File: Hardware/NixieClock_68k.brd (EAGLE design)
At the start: 100 x 100 mm, 80 parts, among them IC1 68008, IC10 7805, IC11 MIC803, IC2 AS6C1008, IC3 39SF020, IC4 DS1244Y, IC5 FT245R, IC6 NE555, IC7 ATF1504AS, IC8 74HC377N, IC9 74HC373N, Q1 2N4401

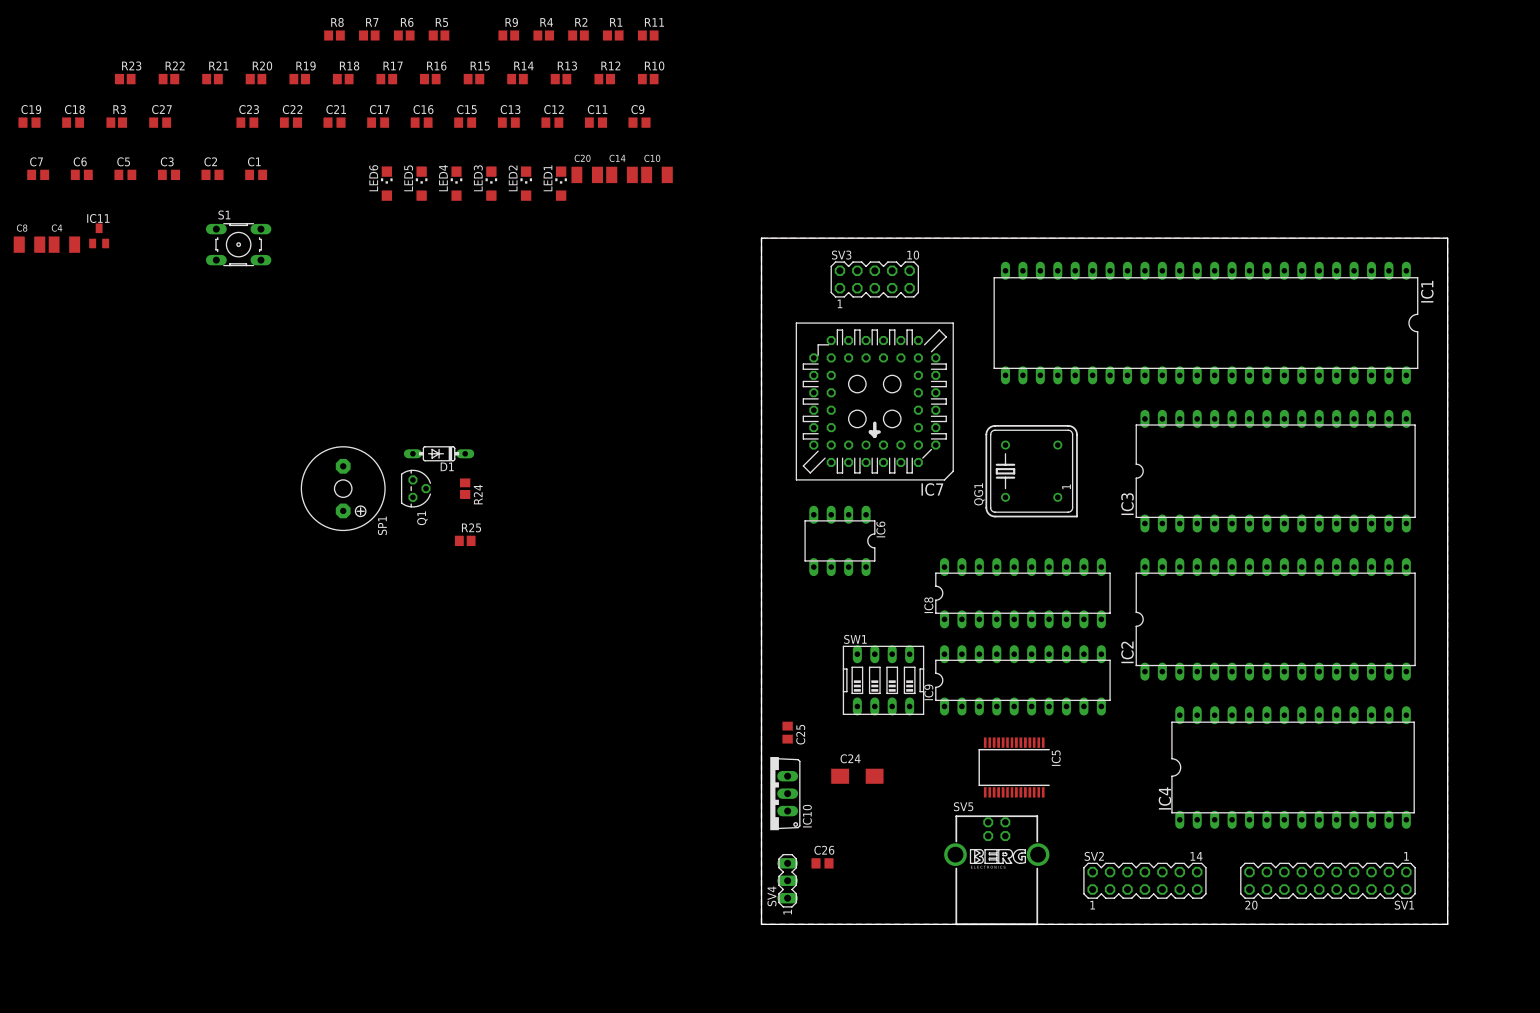
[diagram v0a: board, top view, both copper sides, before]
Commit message: more progress routing board
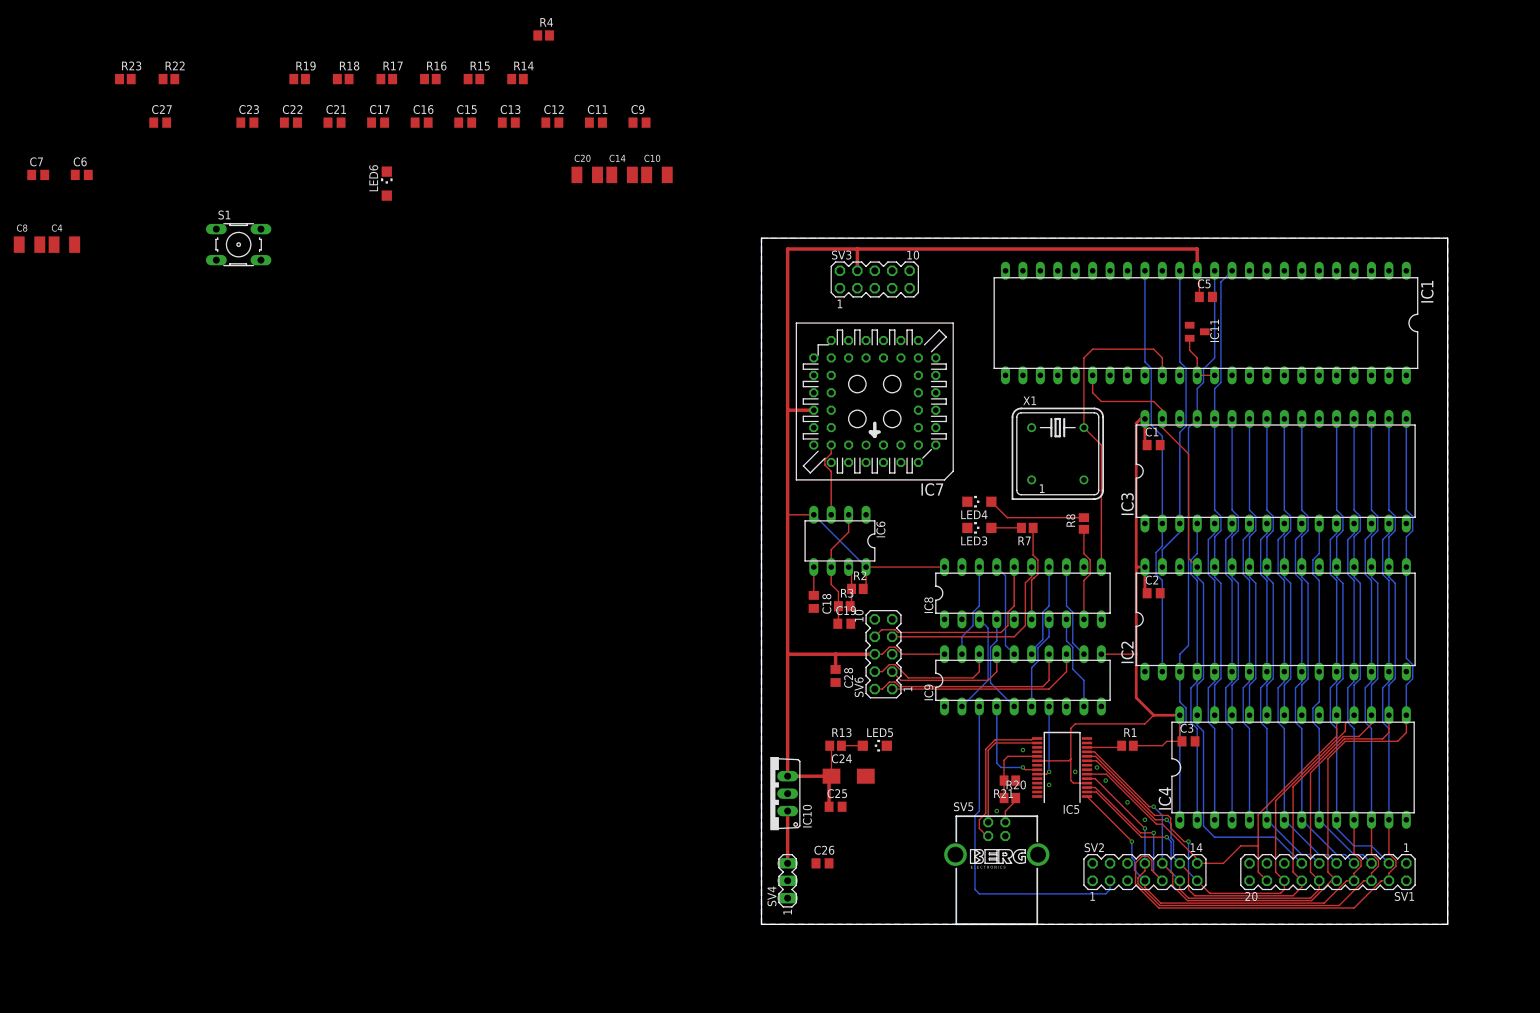
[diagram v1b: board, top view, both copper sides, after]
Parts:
- removed D1: 1N4148, diode:DO35-7
- removed LED1, LED2: (no value), led:CHIPLED_1206
- removed Q1: 2N4401, transistor-npn:TO92
- removed QG1: 4MHz, crystal:DIL08S
- removed R10, R11, R12, R9: 10k, rcl:R2012
- removed R24, R25: 1k, rcl:R2012
- removed R5, R6: 3k, rcl:R2012
- removed SP1: KSS1201, buzzer:KSS1201
- removed SW1: (no value), special:EDG-04
- added C28: 100nF, rcl:C0805
- added SV6: (no value), con-lstb:MA05-2
- added X1: 4MHz, crystal:DIL08S
- moved C3 170.0 mm to (62.2, 26.7)
- moved IC11 160.6 mm to (63.5, 86.4), turned to 270 degrees
- moved C5 158.5 mm to (64.8, 91.4)
- moved R21 154.8 mm to (36.2, 21.0), turned to 180 degrees
- moved R20 151.8 mm to (36.2, 18.4)
- moved C2 150.1 mm to (57.1, 48.3)
- moved C19 139.4 mm to (12.1, 43.8)
- moved C1 136.6 mm to (57.1, 69.8)
- moved R8 130.3 mm to (47.0, 58.4), turned to 90 degrees
- moved C18 128.6 mm to (7.62, 47.0), turned to 270 degrees
- moved R1 127.8 mm to (53.3, 26.0)
- moved R3 127.3 mm to (12.1, 46.4)
- moved R7 119.8 mm to (38.7, 57.8), turned to 180 degrees
- moved LED5 105.2 mm to (16.5, 26.0), turned to 270 degrees
- moved R13 105.1 mm to (10.8, 26.0)
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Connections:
- removed net !IO_OUT_EN: IC7.25
- removed net BEEPER: IC8.16, R24.1
- removed net CFG0: IC9.13, R9.1, SW1.5
- removed net CFG1: IC9.14, R10.1, SW1.6
- removed net CFG2: IC9.17, R11.1, SW1.7
- removed net CFG3: IC9.18, R12.1, SW1.8
- removed net JTAG_TCK: IC7.32
- removed net JTAG_TDI: IC7.7
- removed net JTAG_TDO: IC7.38
- removed net JTAG_TMS: IC7.13
- removed net N$11: Q1.2, R24.2
- removed net N$12: D1.A, Q1.1, SP1.-
- removed net N$13: D1.C, R25.1
- removed net N$3: LED1.A, R5.2
- removed net N$5: LED2.A, R6.2
- removed net VPA: R22.1
- new net OUT0: IC8.16, SV6.8
- new net OUT1: IC8.15, SV6.7
- new net SW0: IC9.13, SV6.1
- new net SW1: IC9.14, SV6.2
- new net SW2: IC9.17, SV6.3
- new net SW3: IC9.18, SV6.4
- net !IO_OUT_CS: now also IC7.25
- net !VPA: now also R22.1
- net +5V: now also C28.1, SV6.6, X1.8; no longer QG1.8, R10.2, R11.2, R12.2, R25.2, R9.2, SP1.+
- net CLK: now also X1.5; no longer QG1.5
- net CPLD_TCK: now also IC7.32
- net CPLD_TDI: now also IC7.7
- net CPLD_TDO: now also IC7.38
- net CPLD_TMS: now also IC7.13
- net D0: now also SV1.8; no longer SV1.4
- net D2: now also SV1.4; no longer SV1.8
- net GND: now also C28.2, IC9.8, SV6.5, X1.4; no longer LED1.C, LED2.C, Q1.3, QG1.4, SW1.1, SW1.2, SW1.3, SW1.4
- net STATUS0: no longer R5.1
- net STATUS1: no longer R6.1
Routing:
- net +5V: track 0.00 -> 323.9 mm
- net D3: track 0.00 -> 144.0 mm, vias 0 -> 1
- net D2: track 0.00 -> 137.9 mm, vias 0 -> 1
- net D4: track 0.00 -> 136.5 mm, vias 0 -> 1
- net D5: track 0.00 -> 134.2 mm, vias 0 -> 1
- net D6: track 0.00 -> 129.8 mm, vias 0 -> 1
- net D1: track 0.00 -> 125.7 mm, vias 0 -> 1
- net D7: track 0.00 -> 119.6 mm
- net D0: track 0.00 -> 118.7 mm, vias 0 -> 1
- net R/!W!: track 0.00 -> 94.2 mm
- net A14: track 0.00 -> 82.9 mm
- net A13: track 0.00 -> 67.3 mm
- net A16: track 0.00 -> 60.2 mm
- net A0: track 0.00 -> 55.7 mm
- net A4: track 0.00 -> 54.9 mm
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
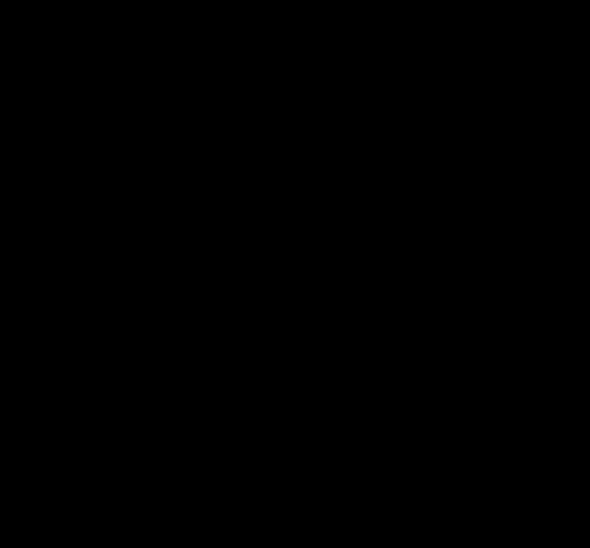
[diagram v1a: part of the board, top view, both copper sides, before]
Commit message: added some more missing pull resistors for usb
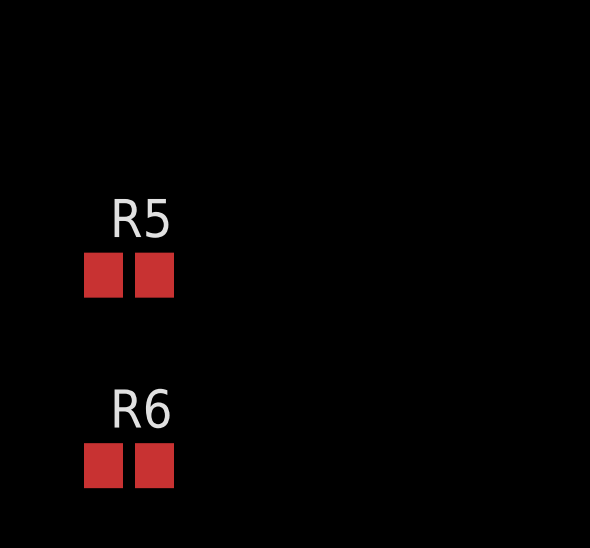
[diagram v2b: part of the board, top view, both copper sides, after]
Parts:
- added R5, R6: 10k, rcl:R2012
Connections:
- net !USB_RXF: now also R6.1
- net !USB_TXE: now also R5.1
- net +5V: now also R6.2
- net GND: now also R5.2
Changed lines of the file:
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@@
 <attribute name="VALUE" x="8.255" y="37.465" size="1.27" layer="27" rot="R270"/>
+</element>
+<element name="R5" library="rcl" library_urn="urn:adsk.eagle:library:334" package="R2012" package3d_urn="urn:adsk.eagle:package:23543/2" value="10k" x="-106.68" y="-3.81" smashed="yes">
+<attribute name="MOUSER" value="652-CR0805FX-1002ELF" x="-106.68" y="-3.81" size="1.778" layer="27" display="off"/>
+<attribute name="NAME" x="-107.315" y="-2.54" size="1.27" layer="25"/>
+<attribute name="SPICEPREFIX" value="R" x="-106.68" y="-3.81" size="1.778" layer="27" display="off"/>
+<attribute name="VALUE" x="-107.315" y="-6.35" size="1.27" layer="27"/>
+</element>
+<element name="R6" library="rcl" library_urn="urn:adsk.eagle:library:334" package="R2012" package3d_urn="urn:adsk.eagle:package:23543/2" value="10k" x="-106.68" y="-10.16" smashed="yes">
+<attribute name="MOUSER" value="652-CR0805FX-1002ELF" x="-106.68" y="-10.16" size="1.778" layer="27" display="off"/>
+<attribute name="NAME" x="-107.315" y="-8.89" size="1.27" layer="25"/>
+<attribute name="SPICEPREFIX" value="R" x="-106.68" y="-10.16" size="1.778" layer="27" display="off"/>
+<attribute name="VALUE" x="-107.315" y="-12.7" size="1.27" layer="27"/>
 </element>
 </elements>
@@
 <wire x1="44.79" y1="23.835" x2="45.085" y2="24.13" width="0.2032" layer="1"/>
 <wire x1="40.19" y1="23.835" x2="44.79" y2="23.835" width="0.2032" layer="1"/>
+<contactref element="R6" pad="2"/>
 <wire x1="63.82" y1="91.44" x2="64.6" y2="86.36" width="0" layer="19" extent="1-1"/>
 <wire x1="17.78" y1="69.85" x2="7.62" y2="74.93" width="0" layer="19" extent="1-1"/>
@@
 <wire x1="-108.18" y1="99.06" x2="-106.36" y2="109.22" width="0" layer="19" extent="1-1"/>
 <wire x1="-103.1" y1="99.06" x2="-108.18" y2="99.06" width="0" layer="19" extent="1-1"/>
+<wire x1="-105.83" y1="-10.16" x2="-108.18" y2="99.06" width="0" layer="19" extent="1-1"/>
 </signal>
 <signal name="GND">
@@
 <via x="34.29" y="16.51" extent="1-16" drill="0.35"/>
 <via x="41.91" y="20.32" extent="1-16" drill="0.35"/>
-<wire x1="-23.18" y1="116.84" x2="-16.83" y2="116.84" width="0" layer="19" extent="1-1"/>
+<contactref element="R5" pad="2"/>
+<wire x1="-105.18" y1="99.06" x2="-105.83" y2="-3.81" width="0" layer="19" extent="1-1"/>
+<wire x1="-100.1" y1="99.06" x2="-105.18" y2="99.06" width="0" layer="19" extent="1-1"/>
+<wire x1="-104.46" y1="109.22" x2="-105.18" y2="99.06" width="0" layer="19" extent="1-1"/>
+<wire x1="-98.11" y1="109.22" x2="-104.46" y2="109.22" width="0" layer="19" extent="1-1"/>
+<wire x1="-86.68" y1="116.84" x2="-98.11" y2="109.22" width="0" layer="19" extent="1-1"/>
+<wire x1="-73.98" y1="116.84" x2="-86.68" y2="116.84" width="0" layer="19" extent="1-1"/>
+<wire x1="-67.63" y1="116.84" x2="-73.98" y2="116.84" width="0" layer="19" extent="1-1"/>
+<wire x1="-61.28" y1="116.84" x2="-67.63" y2="116.84" width="0" layer="19" extent="1-1"/>
+<wire x1="-54.93" y1="116.84" x2="-61.28" y2="116.84" width="0" layer="19" extent="1-1"/>
+<wire x1="-48.58" y1="116.84" x2="-54.93" y2="116.84" width="0" layer="19" extent="1-1"/>
+<wire x1="-42.23" y1="116.84" x2="-48.58" y2="116.84" width="0" layer="19" extent="1-1"/>
+<wire x1="-35.88" y1="116.84" x2="-42.23" y2="116.84" width="0" layer="19" extent="1-1"/>
+<wire x1="-31.43" y1="116.84" x2="-35.88" y2="116.84" width="0" layer="19" extent="1-1"/>
+<wire x1="-53.76" y1="123.19" x2="-54.93" y2="116.84" width="0" layer="19" extent="1-1"/>
+<wire x1="-23.18" y1="116.84" x2="-31.43" y2="116.84" width="0" layer="19" extent="1-1"/>
+<wire x1="-16.83" y1="116.84" x2="-23.18" y2="116.84" width="0" layer="19" extent="1-1"/>
 <wire x1="-23.9" y1="109.22" x2="-23.18" y2="116.84" width="0" layer="19" extent="1-1"/>
 <wire x1="-18.82" y1="109.22" x2="-23.9" y2="109.22" width="0" layer="19" extent="1-1"/>
 <wire x1="-13.74" y1="109.22" x2="-18.82" y2="109.22" width="0" layer="19" extent="1-1"/>
-<wire x1="-31.43" y1="116.84" x2="-23.18" y2="116.84" width="0" layer="19" extent="1-1"/>
-<wire x1="-35.88" y1="116.84" x2="-31.43" y2="116.84" width="0" layer="19" extent="1-1"/>
-<wire x1="-42.23" y1="116.84" x2="-35.88" y2="116.84" width="0" layer="19" extent="1-1"/>
-<wire x1="-48.58" y1="116.84" x2="-42.23" y2="116.84" width="0" layer="19" extent="1-1"/>
-<wire x1="-54.93" y1="116.84" x2="-48.58" y2="116.84" width="0" layer="19" extent="1-1"/>
-<wire x1="-61.28" y1="116.84" x2="-54.93" y2="116.84" width="0" layer="19" extent="1-1"/>
-<wire x1="-67.63" y1="116.84" x2="-61.28" y2="116.84" width="0" layer="19" extent="1-1"/>
-<wire x1="-73.98" y1="116.84" x2="-67.63" y2="116.84" width="0" layer="19" extent="1-1"/>
-<wire x1="-53.76" y1="123.19" x2="-54.93" y2="116.84" width="0" layer="19" extent="1-1"/>
-<wire x1="-86.68" y1="116.84" x2="-73.98" y2="116.84" width="0" layer="19" extent="1-1"/>
-<wire x1="-98.11" y1="109.22" x2="-86.68" y2="116.84" width="0" layer="19" extent="1-1"/>
-<wire x1="-104.46" y1="109.22" x2="-98.11" y2="109.22" width="0" layer="19" extent="1-1"/>
-<wire x1="-105.18" y1="99.06" x2="-104.46" y2="109.22" width="0" layer="19" extent="1-1"/>
-<wire x1="-100.1" y1="99.06" x2="-105.18" y2="99.06" width="0" layer="19" extent="1-1"/>
 <wire x1="-72.9488" y1="96.7994" x2="-73.98" y2="116.84" width="0" layer="19" extent="1-1"/>
 <wire x1="-79.4512" y1="96.7994" x2="-72.9488" y2="96.7994" width="0" layer="19" extent="1-1"/>
@@
 <contactref element="IC1" pad="19"/>
 <contactref element="IC7" pad="9"/>
-<wire x1="25.4" y1="72.39" x2="48.26" y2="95.25" width="0" layer="19" extent="1-1"/>
+<wire x1="48.26" y1="95.25" x2="25.4" y2="72.39" width="0" layer="19" extent="1-1"/>
 </signal>
 <signal name="!IPL1">
@@
 <wire x1="41.91" y1="22.225" x2="41.57" y2="21.885" width="0.2032" layer="1"/>
 <wire x1="41.57" y1="21.885" x2="40.19" y2="21.885" width="0.2032" layer="1"/>
-<wire x1="41.91" y1="31.75" x2="12.7" y2="85.09" width="0" layer="19" extent="1-1"/>
+<contactref element="R6" pad="1"/>
+<wire x1="40.19" y1="21.885" x2="-107.53" y2="-10.16" width="0" layer="19" extent="1-1"/>
+<wire x1="12.7" y1="85.09" x2="41.91" y2="31.75" width="0" layer="19" extent="1-1"/>
 </signal>
 <signal name="!USB_TXE">
@@
 <via x="38.1" y="22.86" extent="1-16" drill="0.35"/>
 <wire x1="38.1" y1="22.86" x2="34.925" y2="22.86" width="0.2032" layer="16"/>
-<wire x1="34.29" y1="31.75" x2="12.7" y2="82.55" width="0" layer="19" extent="1-1"/>
+<contactref element="R5" pad="1"/>
+<wire x1="34.29" y1="23.495" x2="-107.53" y2="-3.81" width="0" layer="19" extent="1-16"/>
+<wire x1="12.7" y1="82.55" x2="34.29" y2="31.75" width="0" layer="19" extent="1-1"/>
 </signal>
 <signal name="USB+">
